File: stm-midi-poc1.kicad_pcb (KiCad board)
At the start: 4 copper layers, 100 x 100 mm, 116 parts, among them CN1 MIDI Out 1, CN2 MIDI In 1, CN3 MIDI Out 2, CN4 MIDI In 2, CN5 Line out, CN6 Headphone, J1 GT-USB-7010I, J2 SWD, J3 I2C, J4 UART456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

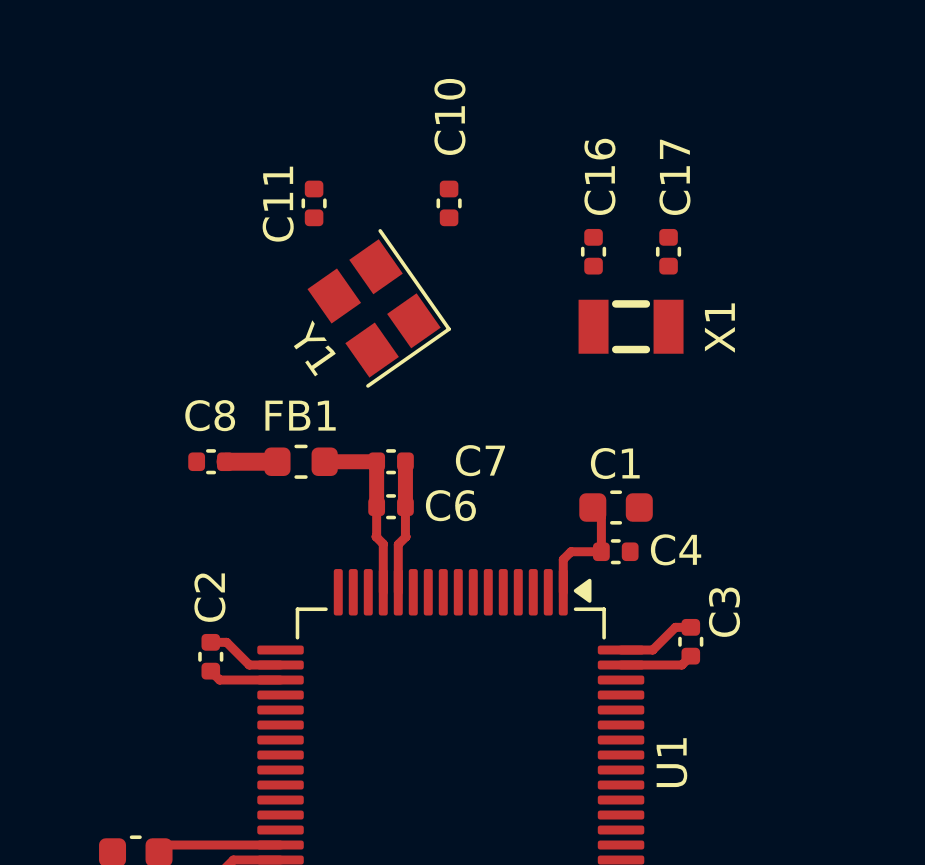
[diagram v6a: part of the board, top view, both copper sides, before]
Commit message: Routed clock signals and addded GND guard.
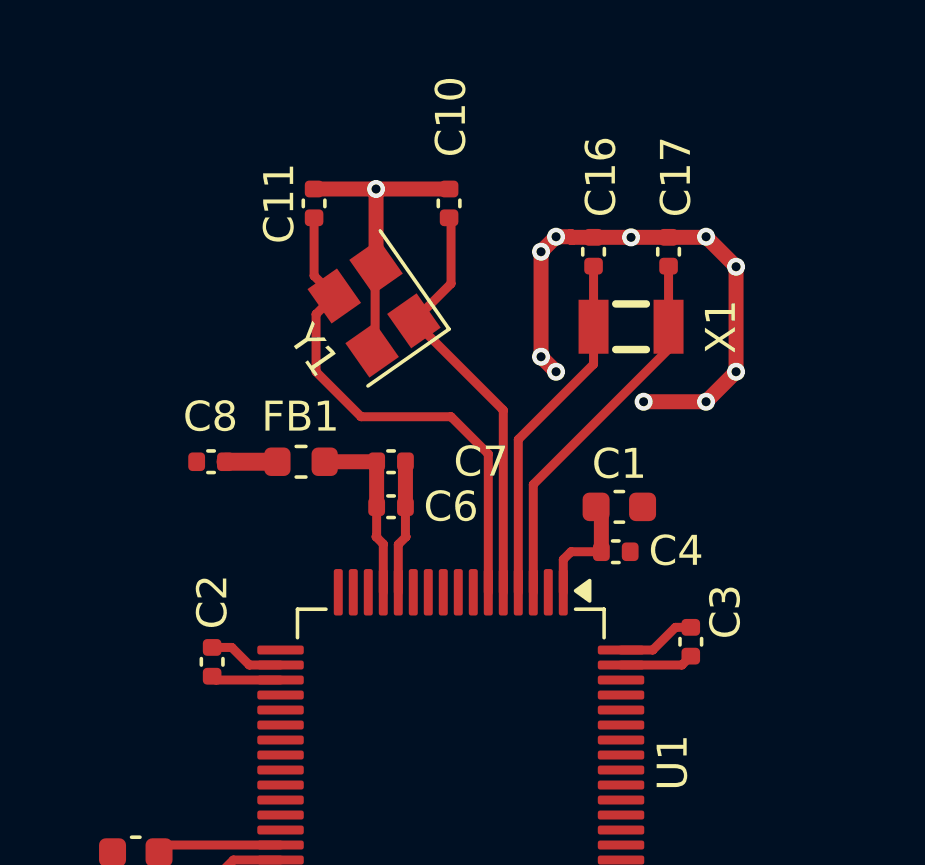
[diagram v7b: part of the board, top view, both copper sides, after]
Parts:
- moved C2 0.18 mm to (163.0, 96.7)
- moved C1 0.11 mm to (176.6, 91.5)
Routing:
- net GND: track 55.0 -> 83.2 mm, vias 2 -> 13
- net /MCU/RCC_OSC_OUT: track 0.00 -> 17.1 mm
- net /MCU/RCC_OSC_IN: track 0.00 -> 14.1 mm
- net /MCU/RCC_OSC32_IN: track 0.00 -> 12.7 mm
- net /MCU/RCC_OSC32_OUT: track 0.00 -> 11.9 mm

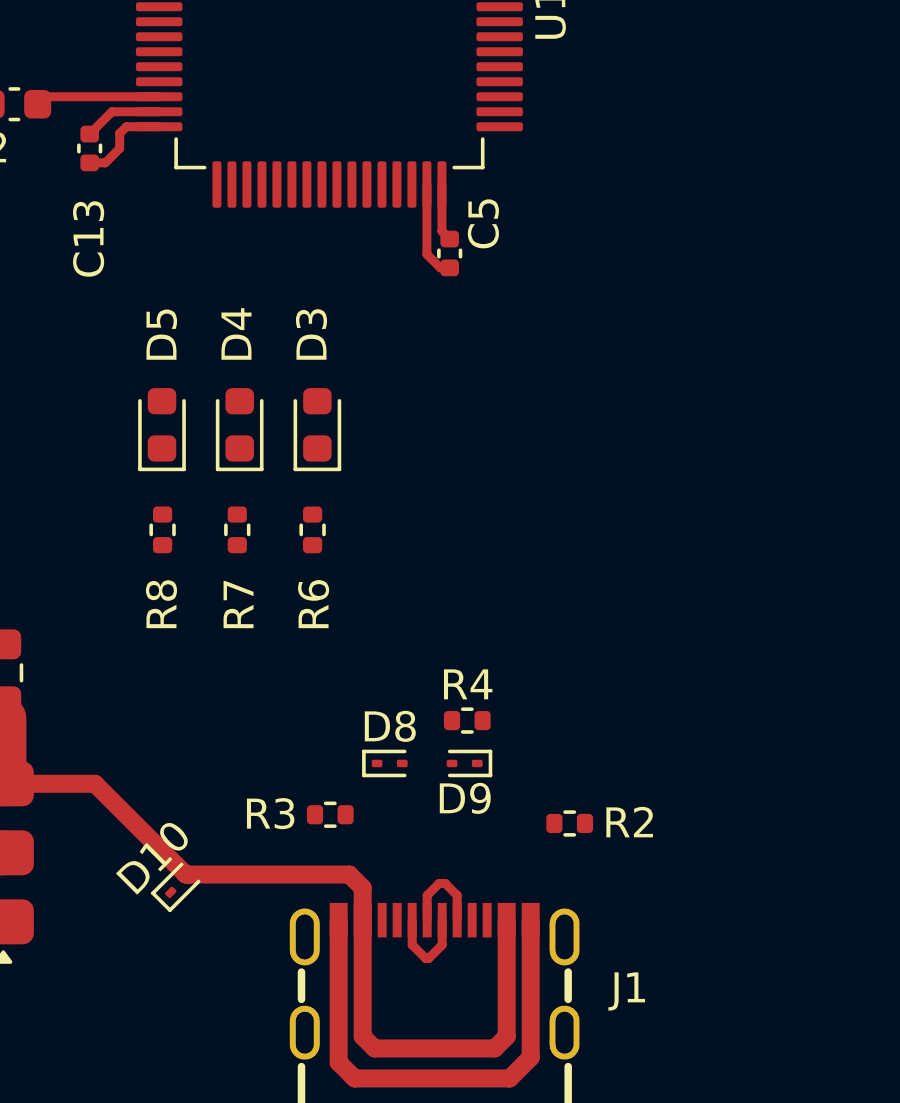
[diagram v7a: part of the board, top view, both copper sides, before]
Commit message: Routed USB signals.
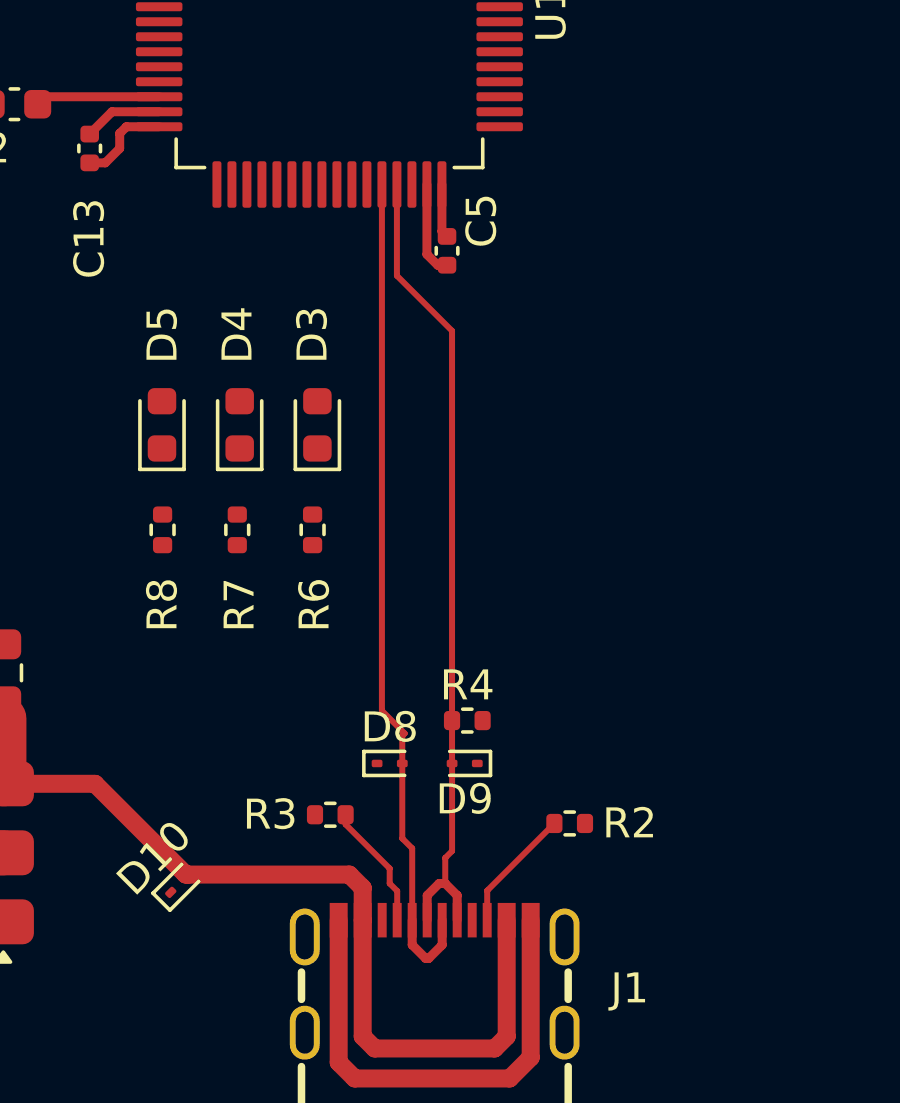
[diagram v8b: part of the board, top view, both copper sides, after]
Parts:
- moved C5 0.13 mm to (174.9, 107.9)
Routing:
- net /MCU/USB_OTG_FS_D-: track 3.02 -> 28.0 mm
- net /MCU/USB_OTG_FS_D+: track 2.98 -> 27.1 mm
- net /MCU/CC1: track 0.00 -> 4.23 mm
- net /MCU/CC2: track 0.00 -> 4.15 mm
- added copper zone on In1.Cu, net GND
- added copper zone on In2.Cu, net GND
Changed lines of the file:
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@@
 	(footprint "Capacitor_SMD:C_0402_1005Metric"
 		(layer "F.Cu")
-		(at 175 108 -90)
+		(at 174.910956 107.911823 -90)
 		(descr "Capacitor SMD 0402 (1005 Metric), square (rectangular) end terminal, IPC_7351 nominal, (Body size source: IPC-SM-782 page 76, https://www.pcb-3d.com/wordpress/wp-content/uploads/ipc-sm-782a_amendment_1_and_2.pdf), generated with kicad-footprint-generator")
 		(tags "capacitor")
@@
 	)
 	(segment
-		(start 174.241181 105.700976)
-		(end 174.241181 108.03118)
-		(width 0.3)
-		(layer "F.Cu")
-		(net 1)
-	)
-	(segment
 		(start 132.741181 88.568476)
 		(end 132.741181 87.582465)
@@
 	)
 	(segment
+		(start 174.241181 105.700976)
+		(end 174.241181 108.03118)
+		(width 0.3)
+		(layer "F.Cu")
+		(net 1)
+	)
+	(segment
 		(start 131.1375 118.275)
 		(end 130.225 118.275)
@@
 	)
 	(segment
+		(start 174.601824 108.391823)
+		(end 174.910956 108.391823)
+		(width 0.3)
+		(layer "F.Cu")
+		(net 1)
+	)
+	(segment
 		(start 168.5 80.908607)
 		(end 168.5 83.5)
@@
 	)
 	(segment
-		(start 174.690001 108.48)
-		(end 175 108.48)
-		(width 0.3)
-		(layer "F.Cu")
-		(net 1)
-	)
-	(segment
 		(start 174 86.5)
 		(end 174.5 87)
@@
 	)
 	(segment
+		(start 174.241181 108.03118)
+		(end 174.601824 108.391823)
+		(width 0.3)
+		(layer "F.Cu")
+		(net 1)
+	)
+	(segment
 		(start 175 82.5)
 		(end 175.02 82.52)
@@
 	)
 	(segment
-		(start 174.241181 108.03118)
-		(end 174.690001 108.48)
-		(width 0.3)
-		(layer "F.Cu")
-		(net 1)
-	)
-	(segment
 		(start 177 82.52)
 		(end 178.25 82.52)
@@
 	)
 	(segment
-		(start 174.741181 107.261181)
-		(end 175 107.52)
-		(width 0.3)
-		(layer "F.Cu")
-		(net 2)
-	)
-	(segment
 		(start 154 122.519657)
 		(end 154.041181 122.478476)
@@
 	)
 	(segment
+		(start 174.741181 107.262048)
+		(end 174.910956 107.431823)
+		(width 0.3)
+		(layer "F.Cu")
+		(net 2)
+	)
+	(segment
 		(start 152 128.5)
 		(end 150.7875 128.5)
@@
 	)
 	(segment
-		(start 174.741181 105.700976)
-		(end 174.741181 107.261181)
-		(width 0.3)
-		(layer "F.Cu")
-		(net 2)
-	)
-	(segment
 		(start 159.761181 65.075976)
 		(end 159.761181 66.275976)
@@
 	)
 	(segment
+		(start 174.741181 105.700976)
+		(end 174.741181 107.262048)
+		(width 0.3)
+		(layer "F.Cu")
+		(net 2)
+	)
+	(segment
 		(start 163.162562 97.275976)
 		(end 163.036385 97.149799)
@@
 	)
 	(segment
+		(start 175.07805 124.99805)
+		(end 175.08 125)
+		(width 0.2)
+		(layer "F.Cu")
+		(net 6)
+	)
+	(segment
+		(start 173.241181 105.700976)
+		(end 173.241181 108.741181)
+		(width 0.2)
+		(layer "F.Cu")
+		(net 6)
+	)
+	(segment
 		(start 174.25 129.398476)
 		(end 174.648476 129)
@@
 	)
 	(segment
+		(start 175.07805 110.57805)
+		(end 175.07805 123.57044)
+		(width 0.2)
+		(layer "F.Cu")
+		(net 6)
+	)
+	(segment
+		(start 175.08 125)
+		(end 175.08 127.92)
+		(width 0.2)
+		(layer "F.Cu")
+		(net 6)
+	)
+	(segment
 		(start 174.648476 129)
 		(end 174.851524 129)
@@
 	)
 	(segment
+		(start 174.851524 128.148476)
+		(end 174.851524 129)
+		(width 0.2)
+		(layer "F.Cu")
+		(net 6)
+	)
+	(segment
 		(start 175.25 129.398476)
 		(end 175.25 130.223476)
@@
 	)
 	(segment
+		(start 175.07805 123.57044)
+		(end 175.07805 124.99805)
+		(width 0.2)
+		(layer "F.Cu")
+		(net 6)
+	)
+	(segment
+		(start 175.08 127.92)
+		(end 174.851524 128.148476)
+		(width 0.2)
+		(layer "F.Cu")
+		(net 6)
+	)
+	(segment
 		(start 174.851524 129)
 		(end 175.25 129.398476)
@@
 	)
 	(segment
+		(start 173.241181 108.741181)
+		(end 175.07805 110.57805)
+		(width 0.2)
+		(layer "F.Cu")
+		(net 6)
+	)
+	(segment
 		(start 166.296985 128.703015)
 		(end 166.203015 128.703015)
@@
 	)
 	(segment
+		(start 173.75 127.83)
+		(end 173.75 130.223476)
+		(width 0.2)
+		(layer "F.Cu")
+		(net 8)
+	)
+	(segment
 		(start 174.298476 131.5)
 		(end 174.201524 131.5)
@@
 	)
 	(segment
+		(start 173.42 124.08)
+		(end 173.42 125)
+		(width 0.2)
+		(layer "F.Cu")
+		(net 8)
+	)
+	(segment
+		(start 173.42 127.5)
+		(end 173.75 127.83)
+		(width 0.2)
+		(layer "F.Cu")
+		(net 8)
+	)
+	(segment
 		(start 174.75 130.223476)
 		(end 174.75 131.048476)
@@
 	)
 	(segment
+		(start 172.741181 105.700976)
+		(end 172.741181 123.241181)
+		(width 0.2)
+		(layer "F.Cu")
+		(net 8)
+	)
+	(segment
+		(start 173.42 125)
+		(end 173.42 127.5)
+		(width 0.2)
+		(layer "F.Cu")
+		(net 8)
+	)
+	(segment
+		(start 173.5 124)
+		(end 173.42 124.08)
+		(width 0.2)
+		(layer "F.Cu")
+		(net 8)
+	)
+	(segment
+		(start 172.741181 123.241181)
+		(end 173.5 124)
+		(width 0.2)
+		(layer "F.Cu")
+		(net 8)
+	)
+	(segment
 		(start 168.741181 92.741181)
 		(end 168.5 92.5)
@@
 		(net 104)
 	)
+	(segment
+		(start 176.25 129.24)
+		(end 178.49 127)
+		(width 0.2)
+		(layer "F.Cu")
+		(net 112)
+	)
+	(segment
+		(start 176.25 130.223476)
+		(end 176.25 129.24)
+		(width 0.2)
+		(layer "F.Cu")
+		(net 112)
+	)
+	(segment
+		(start 173 128.5)
+		(end 171.530545 127.030545)
+		(width 0.2)
+		(layer "F.Cu")
+		(net 113)
+	)
+	(segment
+		(start 173.25 130.223476)
+		(end 173.25 129.25)
+		(width 0.2)
+		(layer "F.Cu")
+		(net 113)
+	)
+	(segment
+		(start 173 129)
+		(end 173 128.5)
+		(width 0.2)
+		(layer "F.Cu")
+		(net 113)
+	)
+	(segment
+		(start 171.530545 127.030545)
+		(end 171.530545 126.708964)
+		(width 0.2)
+		(layer "F.Cu")
+		(net 113)
+	)
+	(segment
+		(start 173.25 129.25)
+		(end 173 129)
+		(width 0.2)
+		(layer "F.Cu")
+		(net 113)
+	)
+	(zone
+		(net 1)
+		(net_name "GND")
+		(layer "In1.Cu")
+		(hatch edge 0.5)
+		(connect_pads
+			(clearance 0.4)
+		)
+		(min_thickness 0.25)
+		(filled_areas_thickness no)
+		(fill yes
+			(thermal_gap 0.5)
+			(thermal_bridge_width 0.5)
+		)
+		(polygon
+			(pts
+				(xy 105 34) (xy 104.5 141) (xy 211 141) (xy 210 33)
+			)
+		)
+	)
+	(zone
+		(net 1)
+		(net_name "GND")
+		(layer "In2.Cu")
+		(hatch edge 0.5)
+		(priority 1)
+		(connect_pads
+			(clearance 0.4)
+		)
+		(min_thickness 0.25)
+		(filled_areas_thickness no)
+		(fill yes
+			(thermal_gap 0.5)
+			(thermal_bridge_width 0.5)
+		)
+		(polygon
+			(pts
+				(xy 104 33) (xy 103.5 141.5) (xy 211.5 141.5) (xy 211.5 32)
+			)
+		)
+	)
 	(group ""
